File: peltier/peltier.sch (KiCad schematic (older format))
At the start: 4 parts

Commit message: Draw joystick
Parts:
- added J?: Joystick module, symbol Connector_Generic:Conn_01x05
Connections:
- net +5V: now also J?.2 (Pin_2)
- net ADC6: now also J?.3 (Pin_3)
- net ADC7: now also J?.4 (Pin_4)
- net GND: now also J?.1 (Pin_1)
- no-connect marks 8 -> 9
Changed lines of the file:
@@
 Wire Wire Line
 	5300 2500 5900 2500
+$Comp
+L Connector_Generic:Conn_01x05 J?
+U 1 1 61FDA9CB
+P 4650 4550
+F 0 "J?" H 4730 4592 50  0000 L CNN
+F 1 "Joystick module" H 4730 4501 50  0000 L CNN
+F 2 "" H 4650 4550 50  0001 C CNN
+F 3 "~" H 4650 4550 50  0001 C CNN
+	1    4650 4550
+	1    0    0    -1
+$EndComp
+$Comp
+L power:GND #PWR?
+U 1 1 61FDAA90
+P 4450 4350
+F 0 "#PWR?" H 4450 4100 50  0001 C CNN
+F 1 "GND" V 4455 4222 50  0000 R CNN
+F 2 "" H 4450 4350 50  0001 C CNN
+F 3 "" H 4450 4350 50  0001 C CNN
+	1    4450 4350
+	0    1    1    0
+$EndComp
+$Comp
+L power:+5V #PWR?
+U 1 1 61FDAB68
+P 4450 4450
+F 0 "#PWR?" H 4450 4300 50  0001 C CNN
+F 1 "+5V" V 4465 4578 50  0000 L CNN
+F 2 "" H 4450 4450 50  0001 C CNN
+F 3 "" H 4450 4450 50  0001 C CNN
+	1    4450 4450
+	0    -1   -1   0
+$EndComp
+NoConn ~ 4450 4750
+Text Label 4450 4550 2    50   ~ 0
+VRX
+Text Label 4450 4650 2    50   ~ 0
+VRY
+Wire Wire Line
+	4450 4550 4100 4550
+Wire Wire Line
+	4450 4650 4100 4650
+Text Label 4100 4650 2    50   ~ 0
+ADC7
+Text Label 4100 4550 2    50   ~ 0
+ADC6
 $EndSCHEMATC

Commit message: Draw thermometer
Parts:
- added U1: DS18B20, Package_TO_SOT_THT:TO-92_Inline, symbol Sensor_Temperature:DS18B20
- gave numbers to parts that had none: 4
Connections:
- net +5V: now also U1.3 (VDD)
- net GND: now also U1.1 (GND)
- net PD7: now also U1.2 (DQ)
- no-connect marks 9 -> 22
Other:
- note added: "DS18B20"
- note added: "JOYSTICK"
- note added: "LCD 1602"
- note added: "NANO3, 16Mhz, 5 V"
- moved on the sheet: A1, DS1, J1, R1, RV1

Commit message: Add documentation
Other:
- note added: "TODO:\n* symbol is unpractical, create a new\nwith ATMEGA ports/pins/alt. functions\ninfo\n* then change net names to correspond\nto peripheral device name"
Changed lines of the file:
@@
 NoConn ~ 1450 3100
 NoConn ~ 1450 3200
-$Comp
-L power:PWR_FLAG #FLG0102
-U 1 1 61FDDBAB
-P 2400 3550
-F 0 "#FLG0102" H 2400 3625 50  0001 C CNN
-F 1 "PWR_FLAG" H 2400 3723 50  0000 C CNN
-F 2 "" H 2400 3550 50  0001 C CNN
-F 3 "~" H 2400 3550 50  0001 C CNN
-	1    2400 3550
-	-1   0    0    1
-$EndComp
 Wire Wire Line
 	1950 3500 1950 3550
 Wire Wire Line
 	2050 3500 2050 3550
-Wire Wire Line
-	2050 3550 2400 3550
-Connection ~ 2050 3550
 $Comp
 L MCU_Module:Arduino_Nano_v3.x A1
@@
 Text Notes 4100 1800 0    157  ~ 0
 DS18B20
+Text Notes 1450 4400 0    39   ~ 0
+TODO:\n* symbol is unpractical, create a new\nwith ATMEGA ports/pins/alt. functions\ninfo\n* then change net names to correspond\nto peripheral device name
+$Comp
+L power:PWR_FLAG #FLG0102
+U 1 1 61FDDBAB
+P 2400 3550
+F 0 "#FLG0102" H 2400 3625 50  0001 C CNN
+F 1 "PWR_FLAG" H 2400 3723 50  0000 C CNN
+F 2 "" H 2400 3550 50  0001 C CNN
+F 3 "~" H 2400 3550 50  0001 C CNN
+	1    2400 3550
+	-1   0    0    1
+$EndComp
+Wire Wire Line
+	2050 3550 2400 3550
+Connection ~ 2050 3550
 $EndSCHEMATC

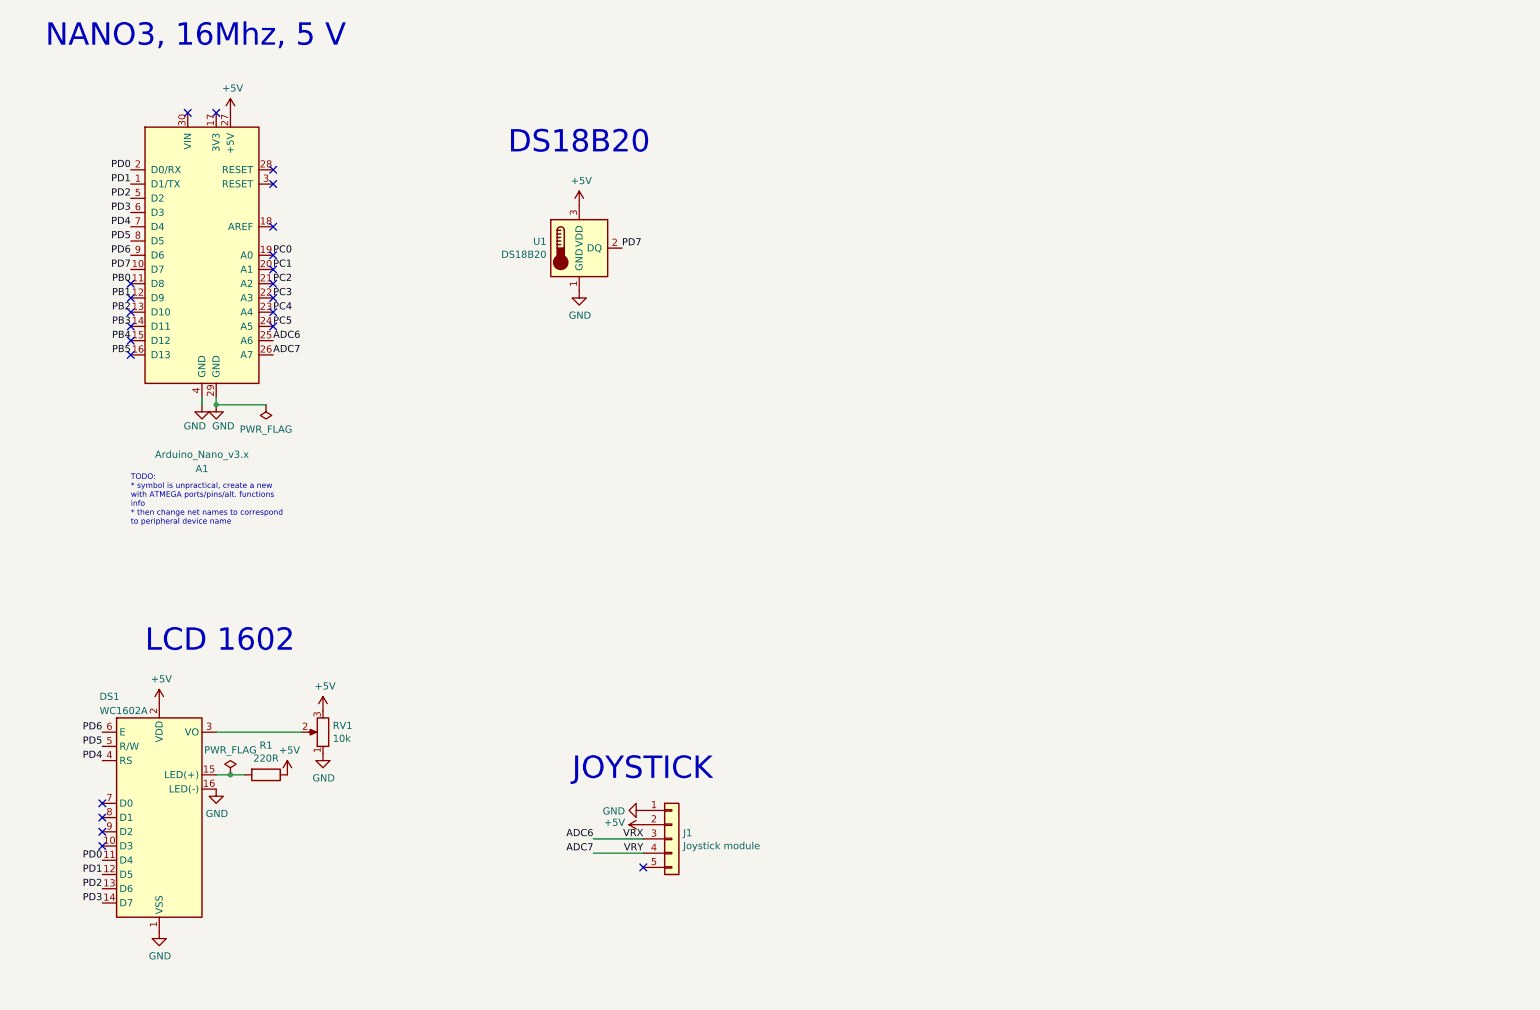
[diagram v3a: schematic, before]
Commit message: Update schematics to full device proposal
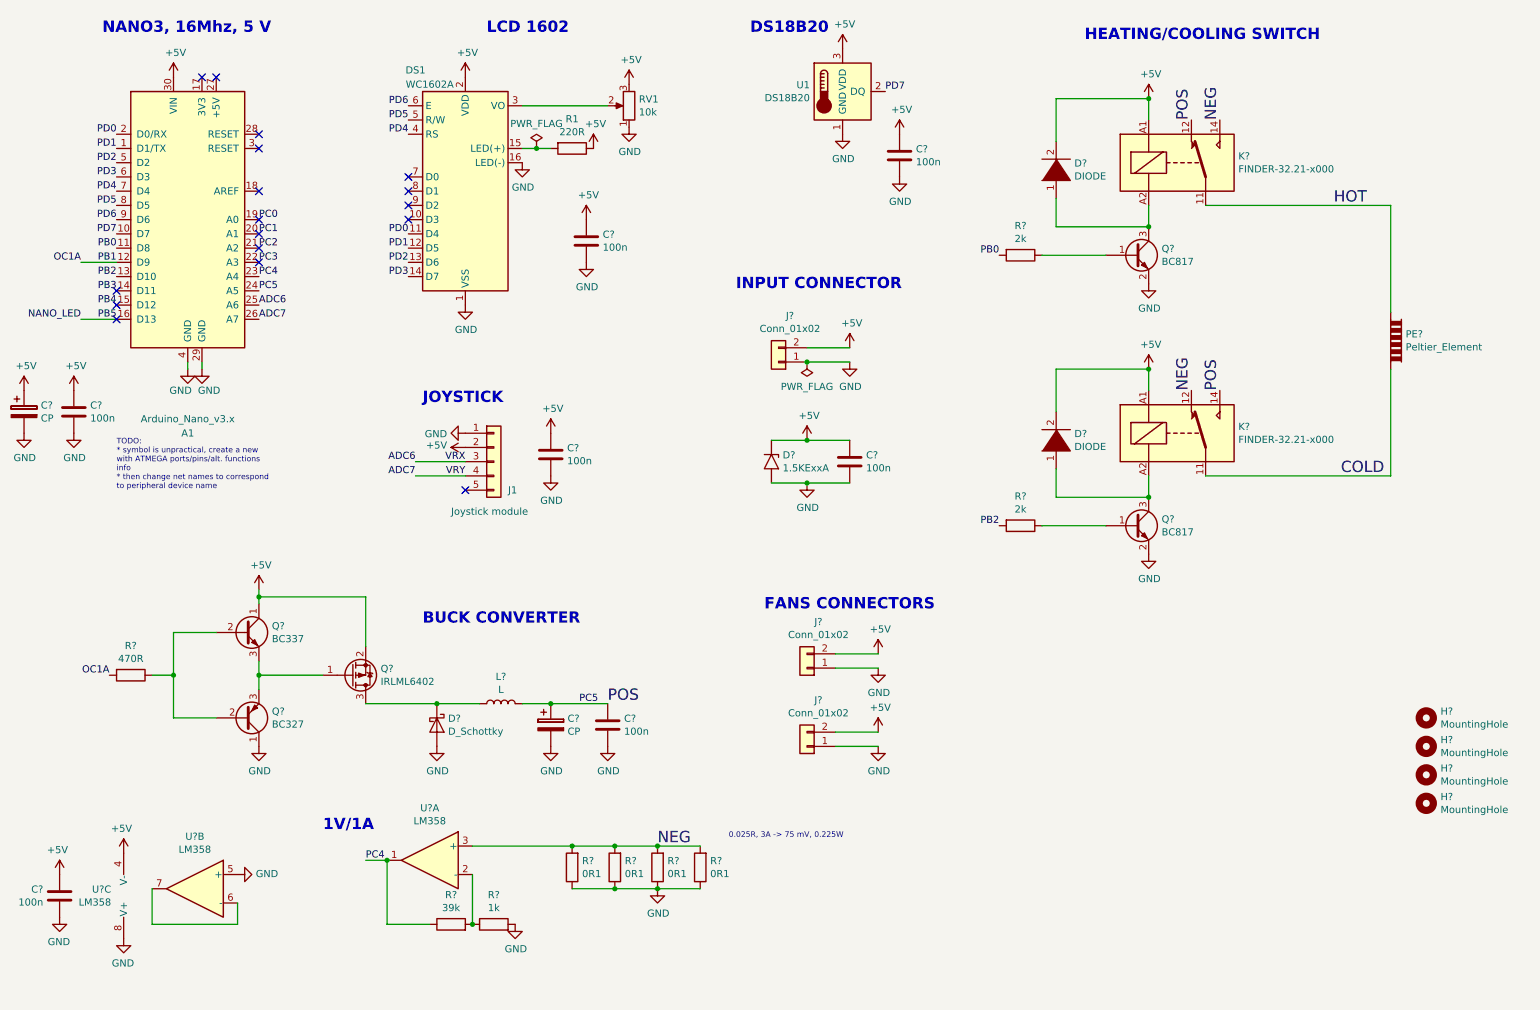
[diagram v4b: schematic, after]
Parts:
- added C? (x2): CP, symbol Device:CP
- added C? (x7): 100n, Capacitor_SMD:C_0805_2012Metric, symbol Device:C
- added D?: D_Schottky, symbol Device:D_Schottky
- added D? (x2): DIODE, symbol pspice:DIODE
- added D?: 1.5KExxA, Diode_THT:D_DO-201AE_P15.24mm_Horizontal, symbol Diode:1.5KExxA
- added H? (x4): MountingHole, symbol Mechanical:MountingHole
- added J? (x3): Conn_01x02, symbol Connector_Generic:Conn_01x02
- added K? (x2): FINDER-32.21-x000, Relay_THT:Relay_SPST_Finder_32.21-x300, symbol Relay:FINDER-32.21-x000
- added L?: L, symbol Device:L
- added PE?: Peltier_Element, symbol Device:Peltier_Element
- added Q?: BC337, Package_TO_SOT_THT:TO-92_Inline, symbol Transistor_BJT:BC337
- added Q?: BC327, Package_TO_SOT_THT:TO-92_Inline, symbol Transistor_BJT:BC327
- added Q? (x2): BC817, Package_TO_SOT_SMD:SOT-23, symbol Transistor_BJT:BC817
- added Q?: IRLML6402, Package_TO_SOT_SMD:SOT-23, symbol Transistor_FET:IRLML6402
- added R?: 470R, symbol Device:R
- added R? (x2): 2k, symbol Device:R
- added R? (x4): 0R1, symbol Device:R
- added R?: 39k, symbol Device:R
- added R?: 1k, symbol Device:R
- added U? (x3): LM358, symbol Amplifier_Operational:LM358
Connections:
- net +5V: now also A1.30 (VIN), C?.1, C?.1, C?.1, C?.1, C?.1, C?.1, C?.1, D?.1 (A1), D?.2 (A), D?.2 (A), J?.2 (Pin_2), J?.2 (Pin_2), J?.2 (Pin_2), K?.A1, K?.A1, Q?.1 (C), Q?.2 (S), U?.4 (V-); no longer A1.27 (+5V)
- net GND: now also C?.2, C?.2, C?.2, C?.2, C?.2, C?.2, C?.2, C?.2, C?.2, D?.2 (A), D?.2 (A2), J?.1 (Pin_1), J?.1 (Pin_1), J?.1 (Pin_1), Q?.1 (C), Q?.2 (E), Q?.2 (E), R?.1, R?.1, R?.1, R?.1, R?.2, U?.5 (+), U?.8 (V+)
- net PB0: now also R?.2
- net PB2: now also R?.2
- net PC4: now also R?.1, U?.1
- net PC5: now also C?.1, C?.1, K?.12, K?.14, L?.2
- net PB1 renamed OC1A
- net OC1A: now also R?.2
- net PB5 renamed NANO_LED
- new net: Q?.2 (B), Q?.2 (B), R?.1
- new net: Q?.1 (G), Q?.3 (E), Q?.3 (E)
- new net: D?.1 (K), L?.1, Q?.3 (D)
- new net: D?.1 (K), K?.A2, Q?.3 (C) (x2)
- new net: Q?.1 (B), R?.1 (x2)
- new net: R?.1, R?.2, U?.2 (-)
- new net: U?.6 (-), U?.7
- new net COLD: K?.11, PE?.1
- new net HOT: K?.11, PE?.2
- new net NEG: K?.12, K?.14, R?.2, R?.2, R?.2, R?.2, U?.3 (+)
- no-connect marks 22 -> 17
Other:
- note added: "0.025R, 3A -> 75 mV, 0.225W"
- note added: "1V/1A"
- note added: "BUCK CONVERTER"
- note added: "FANS CONNECTORS\n"
- note added: "HEATING/COOLING SWITCH"
- note added: "INPUT CONNECTOR\n"
- moved on the sheet: A1, DS1, J1, R1, RV1, U1

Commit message: Update schematics
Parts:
- added C?: 100n, Capacitor_SMD:C_0805_2012Metric, symbol Device:C
- added D?: TL431DBZ, Package_TO_SOT_SMD:SOT-23, symbol Reference_Voltage:TL431DBZ
- added J?: Conn_01x04, symbol Connector_Generic:Conn_01x04
- added Q?: BC327, Package_TO_SOT_THT:TO-92_Inline, symbol Transistor_BJT:BC327
- added Q?: BC337, Package_TO_SOT_THT:TO-92_Inline, symbol Transistor_BJT:BC337
- added R? (x2): Rpu, symbol Device:R
- added R? (x3): 1k, symbol Device:R
- added R?: 20k, symbol Device:R
- added RV?: 1k, symbol Device:R_POT
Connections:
- net +5V: now also J?.2 (Pin_2), Q?.3 (E), R?.1, R?.1, R?.2
- net GND: now also C?.2, D?.3 (A), J?.1 (Pin_1), Q?.3 (E), RV?.3; no longer U?.5 (+)
- net NEG: now also U?.5 (+)
- net PC2: now also C?.1, C?.1, K?.12, K?.14, L?.2
- net PC3: now also R?.1, U?.1
- net PC4: now also J?.3 (Pin_3), R?.2; no longer R?.1, U?.1
- net PC5: now also J?.4 (Pin_4), R?.2; no longer C?.1, C?.1, K?.12, K?.14, L?.2
- net at Q?.2 (B), Q?.2 (B), R?.1: now also Q?.1 (C)
- net at U?.6 (-): now also C?.1, RV?.2; no longer U?.7
- new net: R?.1, U?.7
- new net: Q?.2 (B), R?.1
- new net: Q?.1 (C), R?.2
- new net: Q?.2 (B), R?.2
- new net: D?.1 (K), D?.2 (REF), R?.1, R?.1
- new net: R?.2, RV?.1
- no-connect marks 17 -> 15
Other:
- note added: "0 - 120 mV"
- note added: "I2C CONNECTOR"
- note added: "OVERCURRENT\nPROTECTION"
- moved on the sheet: C?, D?, J?, L?, Q?, R?, U?B, U?C
